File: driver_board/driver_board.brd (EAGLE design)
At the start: 65 x 56 mm, 19 parts, among them Q1 IRLML6346TRPBF, U1 AL5812MP-13

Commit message: picam360
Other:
- board text added: "Picam360"
- board text removed: "OpenBLW"
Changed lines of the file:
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@@
 <wire x1="22" y1="22" x2="21.7" y2="21.7" width="0" layer="20" curve="90"/>
 <wire x1="21.7" y1="21.7" x2="21.7" y2="16.01" width="0" layer="20"/>
-<text x="56.515" y="18.796" size="2.54" layer="21" rot="R90">OpenBLW</text>
+<text x="56.515" y="18.796" size="2.54" layer="21" rot="R90">Picam360</text>
 <text x="59.309" y="19.05" size="1.6764" layer="21" rot="R90">Driver Board</text>
 <text x="61.849" y="19.05" size="1.4224" layer="21" rot="R90">Rev.0.1</text>

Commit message: new camera
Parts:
- moved LOGO1 9.25 mm to (61.5, 32.6), turned to 0 degrees
- moved LED1 7.00 mm to (10.0, 28.0)
- moved LED2 7.00 mm to (55.0, 28.0)
- moved Q1 4.84 mm to (55.2, 15.9)
- moved R1 4.26 mm to (50.8, 15.9), turned to 180 degrees
- moved C1 3.91 mm to (42.3, 19.1), turned to 90 degrees
- moved R2 1.27 mm to (55.9, 12.7), turned to 0 degrees
- moved R3 1.27 mm to (55.9, 10.2), turned to 180 degrees
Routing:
- net N$1: track 38.5 -> 52.2 mm
- net N$9: track 8.69 -> 14.4 mm
- net N$5: track 3.79 -> 5.28 mm
- net VCC: track 77.2 -> 76.0 mm
- added copper zone on layer 16, net VCC
- removed copper zone on layer 1, net VCC
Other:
- outline, holes or cut-outs redrawn
- board text added: "Rev.0.2"
- board text removed: "Rev.0.1"

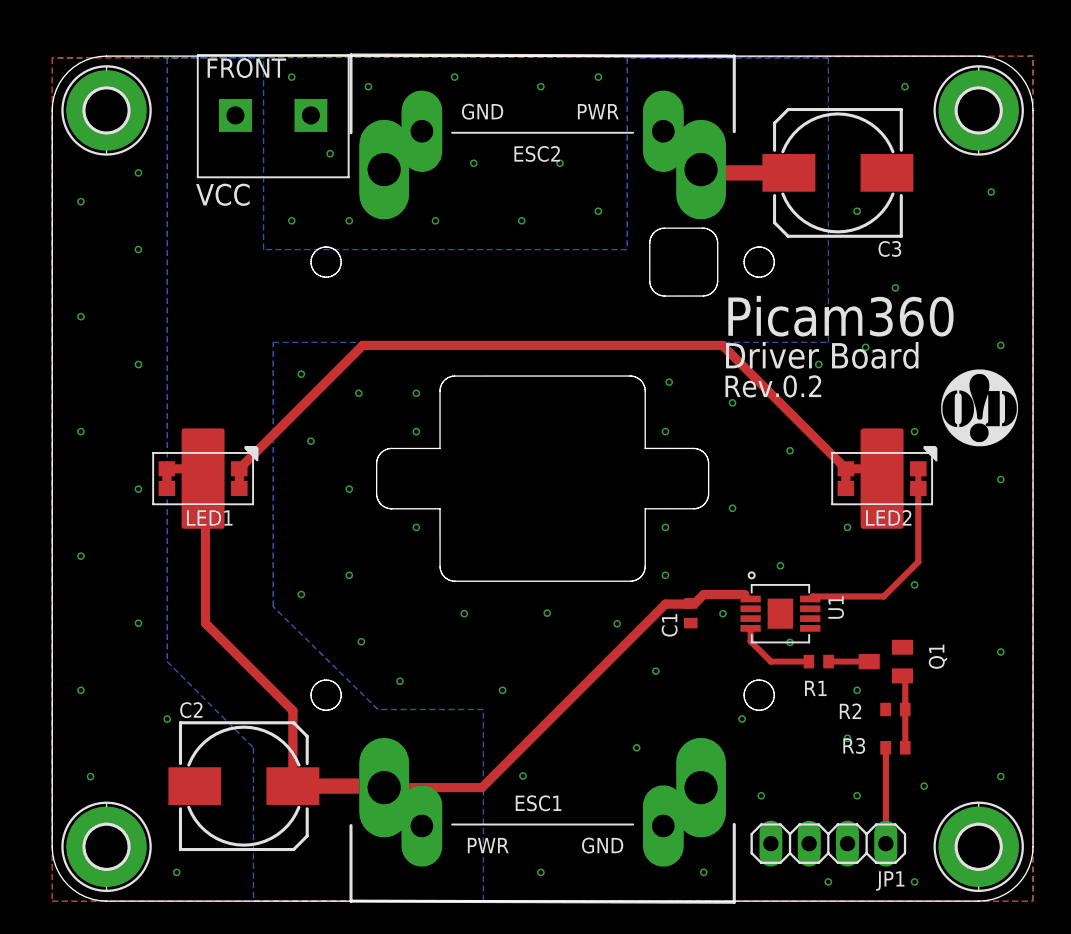
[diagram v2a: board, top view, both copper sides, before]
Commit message: driver board 0.3 not completed
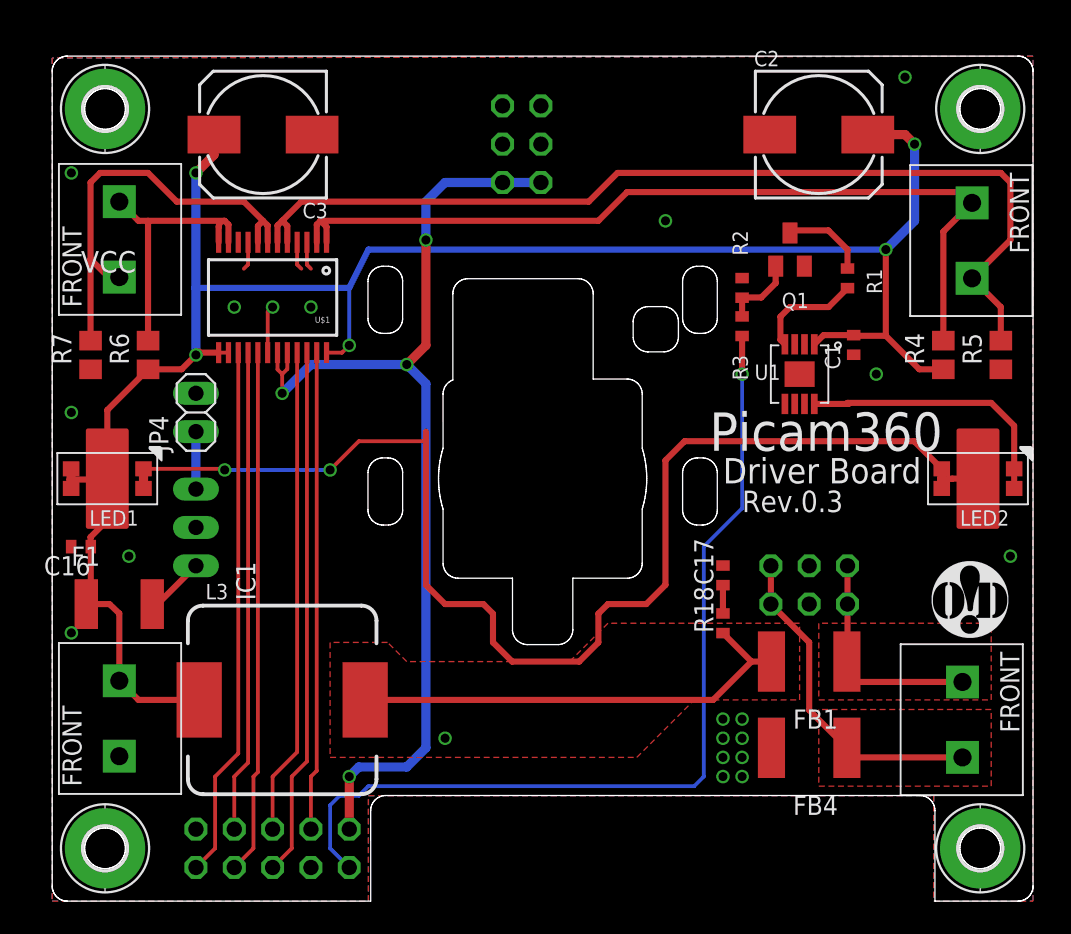
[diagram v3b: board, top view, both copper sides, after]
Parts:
- removed ESC1, ESC2: ESC_POWER, openblw:ESC_POWER
- added C16: 1u, resistor:C0402
- added C17: 10n, resistor:C0402
- added F1: MF-MSMF200-2, openblw:1812
- added FB1, FB4: HR2220V801R-10, resistor:L5650M
- added IC1: V7805-1000, openblw:DIP_3PIN
- added JP2, JP3: M20-9980346, pinhead:2X03
- added JP4: (no value), pinhead:1X02
- added L3: SRP1245A-100M, openblw:SRP1250A
- added R18: 1K, resistor:R0402
- added R4, R5, R6, R7: (no value), resistor:R0805
- added U$2, U$4, U$7, U$8: 282836-2, openblw:282836-2
- added U$3: (no value), openblw:TENDA_P200
- JP1: device pinhead:1X04 -> pinhead:2X05
- U$1: value 282836-2 -> TB6621FNG; device openblw:282836-2 -> openblw:SSOP24
- moved C2 57.6 mm to (50.8, 50.8)
- moved C3 38.2 mm to (14.0, 50.8)
- moved JP1 36.8 mm to (14.6, 3.50), flipped to the bottom, turned to 0 degrees
- moved R2 29.7 mm to (45.7, 40.6), turned to 270 degrees
- moved R3 29.7 mm to (45.7, 38.1), turned to 270 degrees
- moved Q1 28.0 mm to (48.9, 43.2), turned to 0 degrees
- moved R1 25.5 mm to (52.7, 41.3), turned to 270 degrees
- moved C1 20.8 mm to (53.1, 36.9)
- moved U1 15.9 mm to (49.5, 34.9), turned to 180 degrees
- moved LOGO1 12.7 mm to (60.8, 19.9)
- moved U$1 12.1 mm to (14.6, 40.0), turned to 180 degrees
- moved LED2 6.35 mm to (61.4, 28.0)
- moved LED1 6.35 mm to (3.65, 28.0)
- moved H4 0.14 mm to (61.5, 52.5)
- moved H2 0.14 mm to (61.5, 3.50)
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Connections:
- removed net VCC: C1.2, C2.+, C3.+, ESC1.PWR1, ESC1.PWR2, ESC2.PWR1, ESC2.PWR2, LED1.A1, LED1.A2, LED1.A3, U$1.CON1, U1.1
- new net +12V: C1.2, C16.1, C2.+, C3.+, F1.1, L3.2, LED1.A1, LED1.A2, LED1.A3, R4.1, R6.1, U$1.13, U$1.14, U$1.24, U$4.CON2, U1.1
- new net +3V3: JP1.2, JP3.5, JP3.6, U$1.19, U$1.20
- new net +5V: IC1.OUT, JP4.1
- new net AGND: FB4.1, JP2.5, JP2.6, U$2.CON2
- new net AIN1: JP1.6, U$1.21
- new net AIN2: JP1.5, U$1.22
- new net AOUT1: R4.2, U$1.1, U$1.2, U$8.CON1
- new net AOUT2: R5.2, U$1.5, U$1.6, U$8.CON2
- new net AVCC: FB1.1, JP2.1, JP2.2, U$2.CON1
- new net BIN1: JP1.7, U$1.17
- new net BIN2: JP1.8, U$1.16
- new net BOUT1: R6.2, U$1.11, U$1.12, U$7.CON2
- new net BOUT2: R7.2, U$1.7, U$1.8, U$7.CON1
- new net N$3: FB1.2, L3.1, R18.1
- new net N$38: C17.1, R18.2
- new net N$39: F1.2, IC1.IN
- new net PWMA: JP1.4, U$1.23
- new net PWMB: JP1.9, U$1.15
- net GND: now also C16.2, C17.2, FB4.2, IC1.GND, JP1.10, JP1.3, JP3.1, JP4.2, R5.1, R7.1, U$1.10, U$1.18, U$1.3, U$1.4, U$1.9, U$4.CON1; no longer ESC1.GND1, ESC1.GND2, ESC2.GND1, ESC2.GND2, U$1.CON2
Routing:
- net +12V: track 0.00 -> 134.0 mm, vias 0 -> 5
- net VCC: track 76.0 -> 0.00 mm
- net +3V3: track 0.00 -> 68.2 mm, vias 0 -> 4
- net AOUT2: track 0.00 -> 65.3 mm
- net AOUT1: track 0.00 -> 57.3 mm
- net LIGHT_PWM: track 6.36 -> 60.4 mm, vias 0 -> 1
- net PWMB: track 0.00 -> 35.3 mm
- net AIN2: track 0.00 -> 35.1 mm
- net BIN1: track 0.00 -> 34.8 mm
- net N$1: track 52.2 -> 84.9 mm, vias 0 -> 2
- net AIN1: track 0.00 -> 32.3 mm
- net BIN2: track 0.00 -> 32.0 mm
- net PWMA: track 0.00 -> 31.7 mm
- net N$3: track 0.00 -> 30.6 mm
- net BOUT2: track 0.00 -> 29.0 mm
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- added copper zone on layer 1, net AGND
- added copper zone on layer 1, net AVCC
- added copper zone on layer 1, net N$3
- removed copper zone on layer 16, net VCC
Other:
- outline, holes or cut-outs redrawn
- board text added: "Rev.0.3"
- board text removed: "Rev.0.2"

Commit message: driver board 0.3
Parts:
- removed U$1: TB6621FNG, openblw:SSOP24
- added U2: TB6621FNG, openblw:SSOP24
- JP2, JP3: device pinhead:2X03 -> pinhead+:2X03_SMT
- moved FB4 43.0 mm to (43.8, 52.7)
- moved U$2 38.1 mm to (53.3, 49.5), turned to 90 degrees
- moved U$4 38.1 mm to (11.4, 49.5), turned to 270 degrees
- moved L3 37.4 mm to (24.8, 49.5)
- moved U$8 31.8 mm to (59.7, 12.1), turned to 0 degrees
- moved U$7 31.8 mm to (5.08, 12.1), turned to 0 degrees
- moved FB1 31.1 mm to (43.8, 46.4)
- moved R18 26.5 mm to (36.8, 43.8), turned to 180 degrees
- moved C17 24.7 mm to (33.7, 43.8), turned to 180 degrees
- moved C3 22.9 mm to (12.7, 27.9), turned to 270 degrees
- moved C2 22.9 mm to (51.4, 27.9), turned to 270 degrees
- moved F1 22.7 mm to (8.89, 41.9), turned to 180 degrees
- moved IC1 20.4 mm to (5.71, 45.1), turned to 270 degrees
- moved LOGO1 18.5 mm to (45.0, 10.4)
- moved R4 17.9 mm to (57.1, 18.4), turned to 270 degrees
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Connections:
- net +12V: now also U2.13, U2.14, U2.24; no longer U$1.13, U$1.14, U$1.24
- net +3V3: now also U2.19, U2.20; no longer U$1.19, U$1.20
- net AIN1: now also U2.21; no longer U$1.21
- net AIN2: now also U2.22; no longer U$1.22
- net AOUT1: now also U2.1, U2.2; no longer U$1.1, U$1.2
- net AOUT2: now also U2.5, U2.6; no longer U$1.5, U$1.6
- net BIN1: now also U2.17; no longer U$1.17
- net BIN2: now also U2.16; no longer U$1.16
- net BOUT1: now also U2.11, U2.12; no longer U$1.11, U$1.12
- net BOUT2: now also U2.7, U2.8; no longer U$1.7, U$1.8
- net GND: now also U2.10, U2.18, U2.3, U2.4, U2.9; no longer U$1.10, U$1.18, U$1.3, U$1.4, U$1.9
- net PWMA: now also U2.23; no longer U$1.23
- net PWMB: now also U2.15; no longer U$1.15
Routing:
- net +12V: track 134.0 -> 58.1 mm, vias 5 -> 4
- net N$3: track 30.6 -> 0.00 mm
- net BIN1: track 34.8 -> 7.94 mm
- net PWMA: track 31.7 -> 4.91 mm
- net AIN2: track 35.1 -> 8.64 mm
- net BIN2: track 32.0 -> 5.54 mm
- net AIN1: track 32.3 -> 6.05 mm
- net PWMB: track 35.3 -> 9.33 mm
- net LIGHT_PWM: track 60.4 -> 81.0 mm, vias 1 -> 2
- net +3V3: track 68.2 -> 88.5 mm, vias 4 -> 3
- net AOUT1: track 57.3 -> 41.6 mm, vias 0 -> 1
- net AVCC: track 14.8 -> 29.3 mm
- net AGND: track 22.1 -> 36.4 mm
- net AOUT2: track 65.3 -> 52.7 mm, vias 0 -> 1
- net BOUT1: track 18.6 -> 6.95 mm, vias 0 -> 1
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- added copper zone on layer 1, net +12V
- added copper zone on layer 1, net AOUT1
- added copper zone on layer 1, net AOUT2
- added copper zone on layer 1, net BOUT1
- added copper zone on layer 1, net BOUT2
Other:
- outline, holes or cut-outs redrawn
